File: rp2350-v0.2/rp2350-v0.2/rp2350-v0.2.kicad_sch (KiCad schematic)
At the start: 0 parts

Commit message: v0.2: first draft of schematic and footprints
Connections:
- no-connect marks 0 -> 1
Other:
- sheet mcu ports: added none; removed TP_AUX{INT,RESET}
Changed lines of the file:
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@@
 		(color 0 0 0 0)
 	)
-	(bus
-		(pts
-			(xy 147.32 77.47) (xy 160.02 77.47)
-		)
-		(stroke
-			(width 0)
-			(type default)
-		)
+	(no_connect
+		(at 191.77 46.99)
 	)
 	(bus
@@
 	(bus
 		(pts
-			(xy 160.02 46.99) (xy 210.82 46.99)
+			(xy 191.77 46.99) (xy 210.82 46.99)
 		)
 		(stroke
@@
 		(pts
 			(xy 62.23 71.12) (xy 88.9 71.12)
-		)
-		(stroke
-			(width 0)
-			(type default)
-		)
-	)
-	(bus
-		(pts
-			(xy 160.02 77.47) (xy 160.02 46.99)
 		)
 		(stroke
@@
 			)
 		)
-		(pin "TP_AUX{INT,RESET}" output
-			(at 147.32 77.47 0)
-			(effects
-				(font
-					(size 1.27 1.27)
-				)
-				(justify right)
-			)
-		)

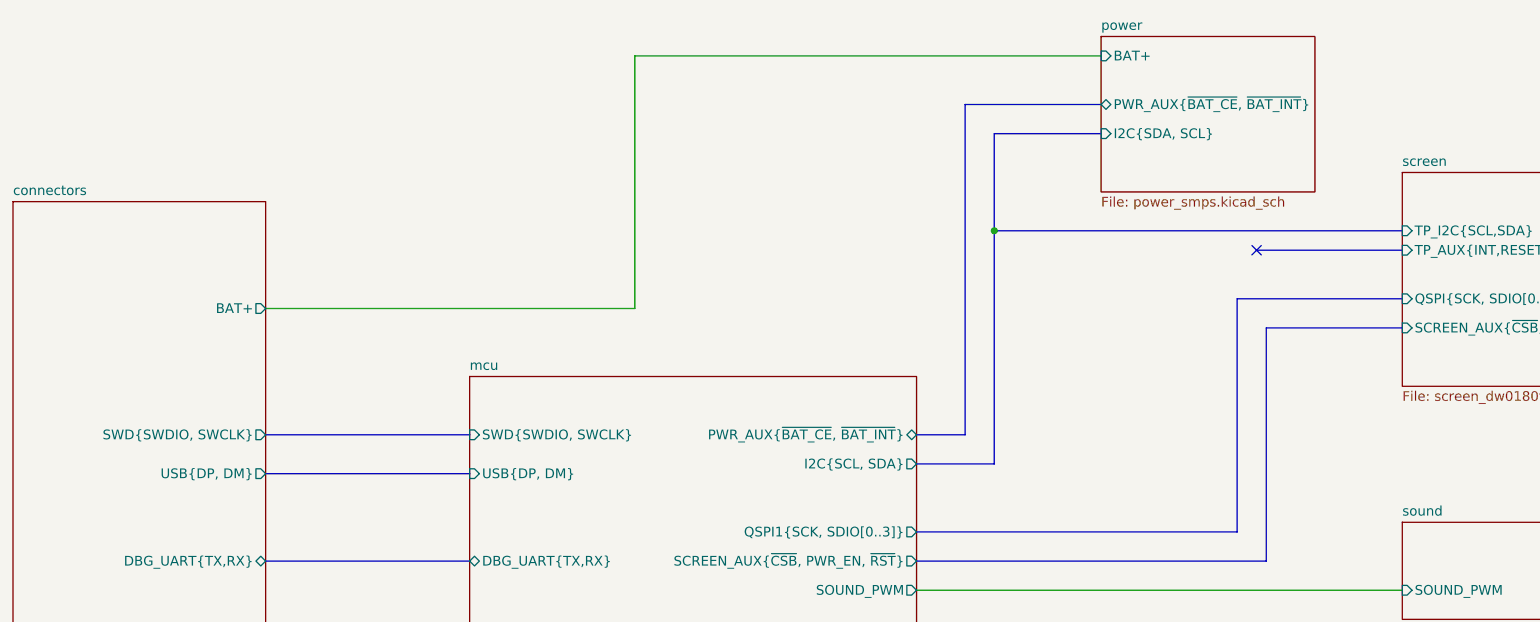
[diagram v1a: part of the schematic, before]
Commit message: v0.2: more progress on routing, nearly done
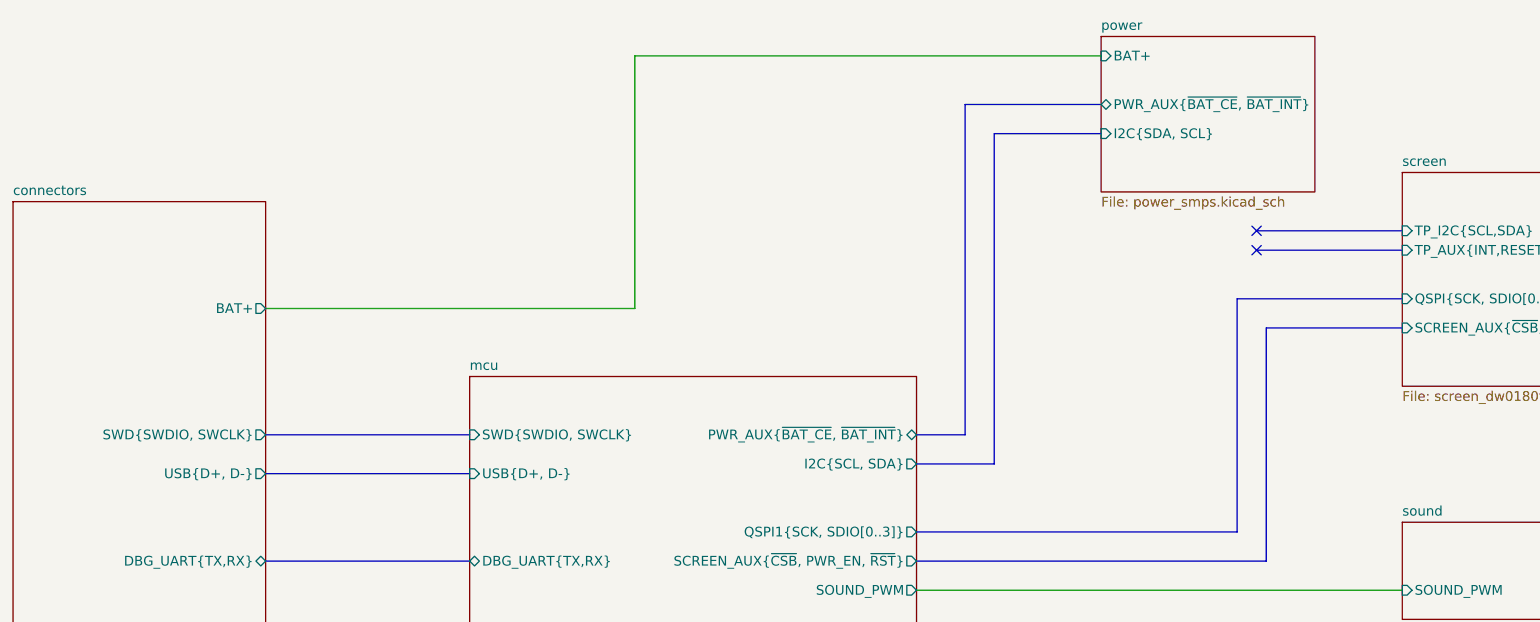
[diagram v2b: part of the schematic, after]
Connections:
- no-connect marks 1 -> 2
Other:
- sheet connectors ports: added USB{D+, D-}; removed USB{DP, DM}
- sheet mcu ports: added USB{D+, D-}; removed USB{DP, DM}
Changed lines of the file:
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@@
 	(paper "A4")
-	(junction
-		(at 157.48 44.45)
-		(diameter 0)
-		(color 0 0 0 0)
-	)
 	(junction
 		(at 168.91 147.32)
@@
 		(at 191.77 46.99)
 	)
+	(no_connect
+		(at 191.77 44.45)
+	)
 	(bus
 		(pts
@@
 	(bus
 		(pts
-			(xy 210.82 44.45) (xy 157.48 44.45)
-		)
-		(stroke
-			(width 0)
-			(type default)
-		)
-	)
-	(bus
-		(pts
 			(xy 193.04 57.15) (xy 210.82 57.15)
 		)
@@
 	(bus
 		(pts
-			(xy 157.48 44.45) (xy 157.48 74.93)
-		)
-		(stroke
-			(width 0)
-			(type default)
-		)
-	)
-	(bus
-		(pts
 			(xy 147.32 147.32) (xy 168.91 147.32)
 		)
@@
 	(bus
 		(pts
+			(xy 191.77 44.45) (xy 210.82 44.45)
+		)
+		(stroke
+			(width 0)
+			(type default)
+		)
+	)
+	(bus
+		(pts
 			(xy 153.67 27.94) (xy 171.45 27.94)
 		)
@@
 	(bus
 		(pts
-			(xy 157.48 31.75) (xy 157.48 44.45)
+			(xy 157.48 31.75) (xy 157.48 74.93)
 		)
 		(stroke
@@
 			)
 		)
-		(pin "USB{DP, DM}" input
-			(at 88.9 76.2 180)
-			(effects
-				(font
-					(size 1.27 1.27)
-				)
-				(justify left)
-			)
-		)
 		(pin "IRDA{TX, RX, SD}" output
 			(at 147.32 107.95 0)
@@
 		(pin "QSPI0{SS, SCLK, SD[0..3]}" bidirectional
 			(at 88.9 115.57 180)
+			(effects
+				(font
+					(size 1.27 1.27)
+				)
+				(justify left)
+			)
+		)
+		(pin "USB{D+, D-}" input
+			(at 88.9 76.2 180)
 			(effects
 				(font
@@
 			)
 		)
-		(pin "USB{DP, DM}" output
+		(pin "USB{D+, D-}" output
 			(at 62.23 76.2 0)
 			(effects
